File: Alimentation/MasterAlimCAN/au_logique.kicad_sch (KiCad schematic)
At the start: 7 parts, among them J10 Conn AU, J8 Conn AU

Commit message: Init placement for MasterAlimCAN
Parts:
- renumbered D6 to D5, D7 to D6, J10 to J9, R14 to R13, R15 to R14, R16 to R15

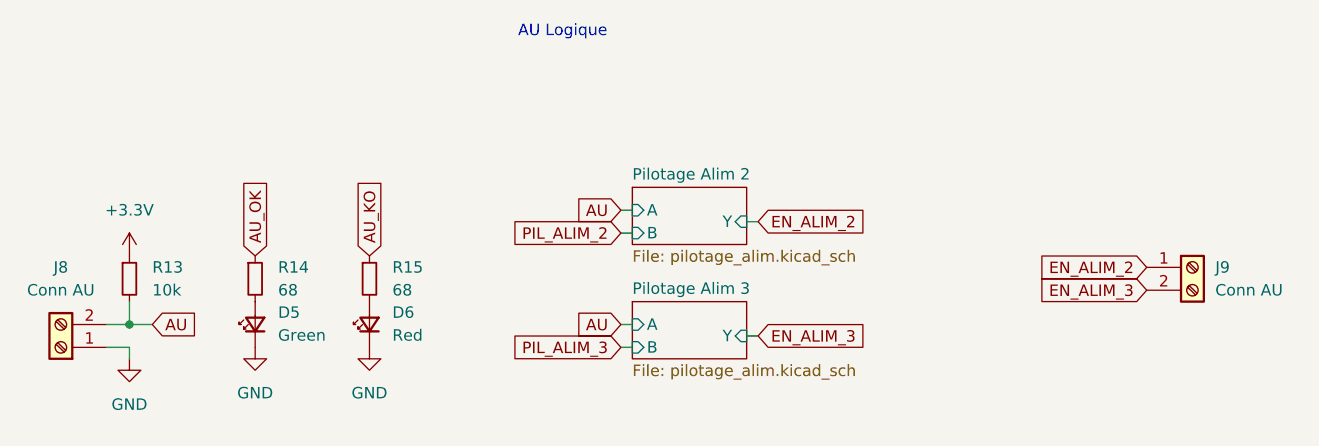
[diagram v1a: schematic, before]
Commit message: New placement for Alim
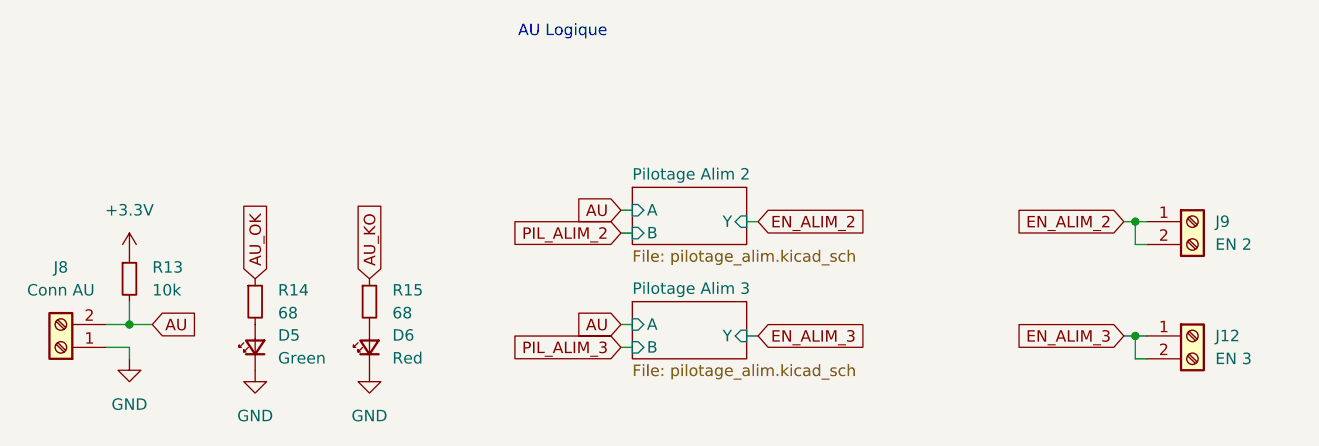
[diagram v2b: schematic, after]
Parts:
- added J12: EN 3, TerminalBlock_Phoenix:TerminalBlock_Phoenix_MPT-0,5-2-2.54_1x02_P2.54mm_Horizontal, symbol Connector:Screw_Terminal_01x02
- J9: value Conn AU -> EN 2
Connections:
- net EN_ALIM_2: now also J9.2 (Pin_2)
- net EN_ALIM_3: now also J12.1 (Pin_1), J12.2 (Pin_2); no longer J9.2 (Pin_2)
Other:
- moved on the sheet: D5, D6, J9, R14, R15
